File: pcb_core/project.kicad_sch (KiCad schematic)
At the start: 55 parts, among them IC4 TCA9548APWR, J1 Conn_01x02, J19 Conn_02x02_Counter_Clockwise, J2 1725656, J20 PCBConnector, J21 PCBConnector, J22 PCBConnector, J23 PCBConnector, J25 PCBConnector, J27 PCBConnector, Q1 SI9945BDY-T1-GE3, U1 ESP32-S3-WROOM-2, U2 LTC4365TS8, U3 ESP32-DevKitC

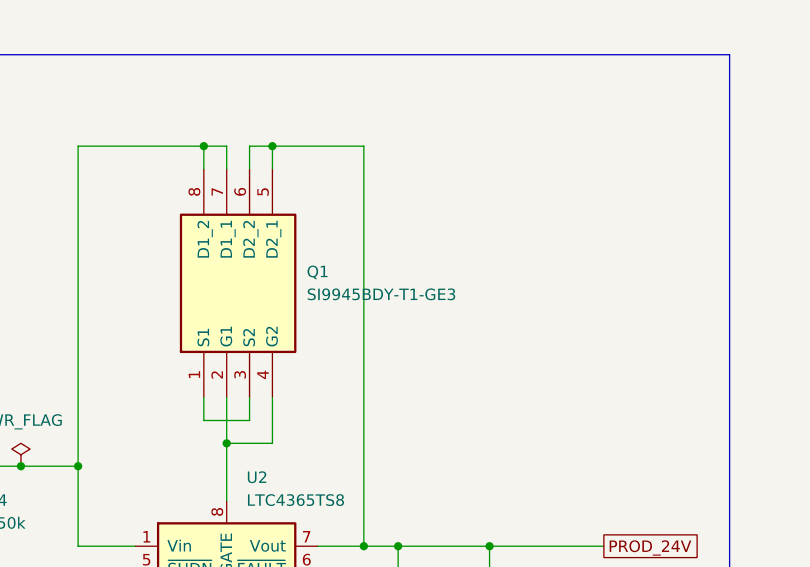
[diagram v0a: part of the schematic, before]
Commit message: Change to I4214DDY-T1-GE3 and update PCB
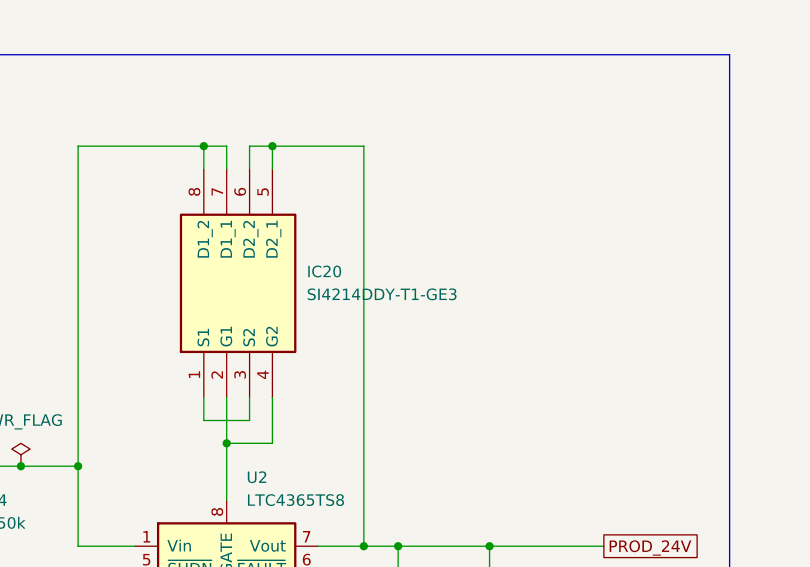
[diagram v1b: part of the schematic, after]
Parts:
- removed Q1: SI9945BDY-T1-GE3, library:SOIC127P600X175-8N, symbol SI9945BDY-T1-GE3:SI9945BDY-T1-GE3
- added IC20: SI4214DDY-T1-GE3, library:SOIC127P600X175-8N, symbol SI4214DDY-T1-GE3:SI4214DDY-T1-GE3
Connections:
- net PROD_24V: now also IC20.5 (D2_1), IC20.6 (D2_2)
- net VIN_24V: now also IC20.7 (D1_1), IC20.8 (D1_2)
- net at U2.8 (GATE): now also IC20.2 (G1), IC20.4 (G2)
- new net: IC20.1 (S1), IC20.3 (S2)
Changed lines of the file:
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@@
 	)
 	(symbol
+		(lib_id "SI4214DDY-T1-GE3:SI4214DDY-T1-GE3")
+		(at 140.97 344.17 90)
+		(unit 1)
+		(exclude_from_sim no)
+		(in_bom yes)
+		(on_board yes)
+		(dnp no)
+		(fields_autoplaced yes)
+		(property "Reference" "IC20"
+			(at 152.4 330.1999 90)
+			(effects
+				(font
+					(size 1.27 1.27)
+				)
+				(justify right)
+			)
+		)
+		(property "Value" "SI4214DDY-T1-GE3"
+			(at 152.4 332.7399 90)
+			(effects
+				(font
+					(size 1.27 1.27)
+				)
+				(justify right)
+			)
+		)
+		(property "Footprint" "library:SOIC127P600X175-8N"
+			(at 235.89 322.58 0)
+			(effects
+				(font
+					(size 1.27 1.27)
+				)
+				(justify left top)
+				(hide yes)
+			)
+		)
+		(property "Datasheet" "https://www.vishay.com/docs/65022/si4214ddy.pdf"
+			(at 335.89 322.58 0)
+			(effects
+				(font
+					(size 1.27 1.27)
+				)
+				(justify left top)
+				(hide yes)
+			)
+		)
+		(property "Description" "SI4214DDY-T1-GE3, Dual N-channel MOSFET Transistor 7.5A 30V, 8-Pin SOIC"
+			(at 140.97 344.17 0)
+			(effects
+				(font
+					(size 1.27 1.27)
+				)
+				(hide yes)
+			)
+		)
+		(property "Height" "1.75"
+			(at 535.89 322.58 0)
+			(effects
+				(font
+					(size 1.27 1.27)
+				)
+				(justify left top)
+				(hide yes)
+			)
+		)
+		(property "Mouser Part Number" "781-SI4214DDY-GE3"
+			(at 635.89 322.58 0)
+			(effects
+				(font
+					(size 1.27 1.27)
+				)
+				(justify left top)
+				(hide yes)
+			)
+		)
+		(property "Mouser Price/Stock" "https://www.mouser.co.uk/ProductDetail/Vishay-Semiconductors/SI4214DDY-T1-GE3?qs=kt16UJ73eEGZKWuc2RKrng%3D%3D"
+			(at 735.89 322.58 0)
+			(effects
+				(font
+					(size 1.27 1.27)
+				)
+				(justify left top)
+				(hide yes)
+			)
+		)
+		(property "Manufacturer_Name" "Vishay"
+			(at 835.89 322.58 0)
+			(effects
+				(font
+					(size 1.27 1.27)
+				)
+				(justify left top)
+				(hide yes)
+			)
+		)
+		(property "Manufacturer_Part_Number" "SI4214DDY-T1-GE3"
+			(at 935.89 322.58 0)
+			(effects
+				(font
+					(size 1.27 1.27)
+				)
+				(justify left top)
+				(hide yes)
+			)
+		)
+		(property "LCSC#" "C553963"
+			(at 140.97 344.17 0)
+			(effects
+				(font
+					(size 1.27 1.27)
+				)
+				(hide yes)
+			)
+		)
+		(property "Config" "-SubNode "
+			(at 140.97 344.17 0)
+			(effects
+				(font
+					(size 1.27 1.27)
+				)
+				(hide yes)
+			)
+		)
+		(pin "6"
+		)
+		(pin "7"
+		)
+		(pin "1"
+		)
+		(pin "4"
+		)
+		(pin "3"
+		)
+		(pin "2"
+		)
+		(pin "8"
+		)
+		(pin "5"
+		)
+		(instances
+			(project "project"
+				(path "/97ee99f6-6664-45d1-b5d6-247aaf34e934"
+					(reference "IC20")
+					(unit 1)
+				)
+			)
+		)
+	)
+	(symbol
 		(lib_id "power:PWR_FLAG")
 		(at 120.65 25.4 0)
@@
 					(unit 1)
 				)
-			)
-		)
-	)
-	(symbol
-		(lib_id "SI9945BDY-T1-GE3:SI9945BDY-T1-GE3")
-		(at 140.97 344.17 90)
-		(unit 1)
-		(exclude_from_sim no)
-		(in_bom yes)
-		(on_board yes)
-		(dnp no)
-		(fields_autoplaced yes)
-		(property "Reference" "Q1"
-			(at 152.4 330.1999 90)
-			(effects
-				(font
-					(size 1.27 1.27)
-				)
-				(justify right)
-			)
-		)
-		(property "Value" "SI9945BDY-T1-GE3"
-			(at 152.4 332.7399 90)
-			(effects
-				(font
-					(size 1.27 1.27)
-				)
-				(justify right)
-			)
-		)
-		(property "Footprint" "library:SOIC127P600X175-8N"
-			(at 235.89 322.58 0)
-			(effects
-				(font
-					(size 1.27 1.27)
-				)
-				(justify left top)
-				(hide yes)
-			)
-		)
-		(property "Datasheet" ""
-			(at 335.89 322.58 0)
-			(effects
-				(font
-					(size 1.27 1.27)
-				)
-				(justify left top)
-				(hide yes)
-			)
-		)
-		(property "Description" "Vishay SI9945BDY-T1-GE3 Dual N-channel MOSFET Transistor, 5.3 A, 60 V, 8-Pin SOIC"
-			(at 140.97 344.17 0)
-			(effects
-				(font
-					(size 1.27 1.27)
-				)
-				(hide yes)
-			)
-		)
-		(property "Height" "1.75"
-			(at 535.89 322.58 0)
-			(effects
-				(font
-					(size 1.27 1.27)
-				)
-				(justify left top)
-				(hide yes)
-			)
-		)
-		(property "Mouser Part Number" "781-SI9945BDY-GE3"
-			(at 635.89 322.58 0)
-			(effects
-				(font
-					(size 1.27 1.27)
-				)
-				(justify left top)
-				(hide yes)
-			)
-		)
-		(property "Manufacturer_Name" "Vishay"
-			(at 835.89 322.58 0)
-			(effects
-				(font
-					(size 1.27 1.27)
-				)
-				(justify left top)
-				(hide yes)
-			)
-		)
-		(property "Manufacturer_Part_Number" "SI9945BDY-T1-GE3"
-			(at 935.89 322.58 0)
-			(effects
-				(font
-					(size 1.27 1.27)
-				)
-				(justify left top)
-				(hide yes)
-			)
-		)
-		(property "LCSC#" "C435838"
-			(at 140.97 344.17 0)
-			(effects
-				(font
-					(size 1.27 1.27)
-				)
-				(hide yes)
-			)
-		)
-		(property "Config" "-SubNode "
-			(at 140.97 344.17 0)
-			(effects
-				(font
-					(size 1.27 1.27)
-				)
-				(hide yes)
-			)
-		)
-		(property "LCSC# Alt1" ""
-			(at 140.97 344.17 0)
-			(effects
-				(font
-					(size 1.27 1.27)
-				)
-				(hide yes)
-			)
-		)
-		(pin "8"
-		)
-		(pin "7"
-		)
-		(pin "6"
-		)
-		(pin "5"
-		)
-		(pin "1"
-		)
-		(pin "4"
-		)
-		(pin "3"
-		)
-		(pin "2"
-		)
-		(instances
-			(project "project"
-				(path "/97ee99f6-6664-45d1-b5d6-247aaf34e934"
-					(reference "Q1")
-					(unit 1)
-				)

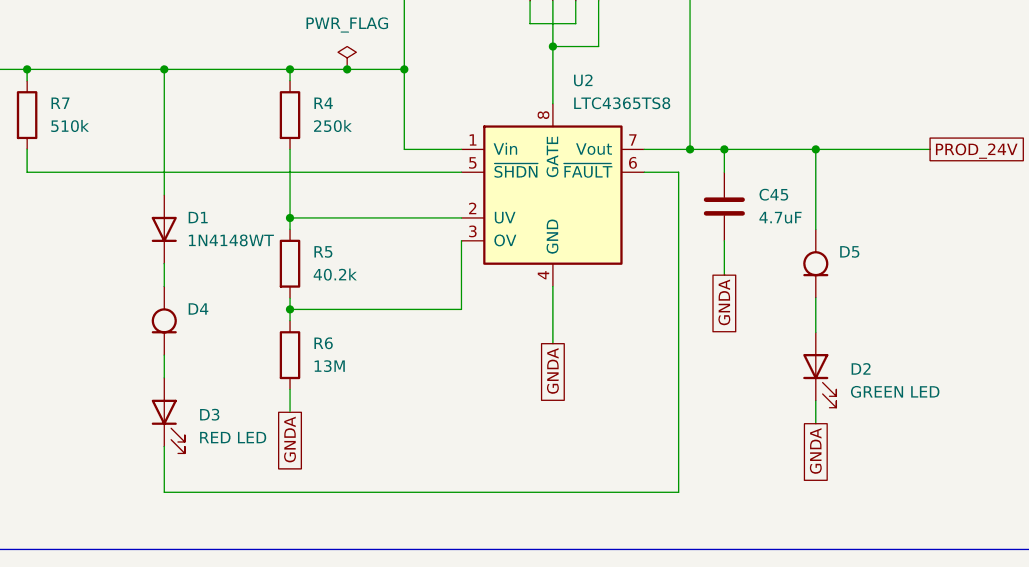
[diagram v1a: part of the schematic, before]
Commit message: Correct schematic symbol for Current Regulator Diodes, Update Kibot config
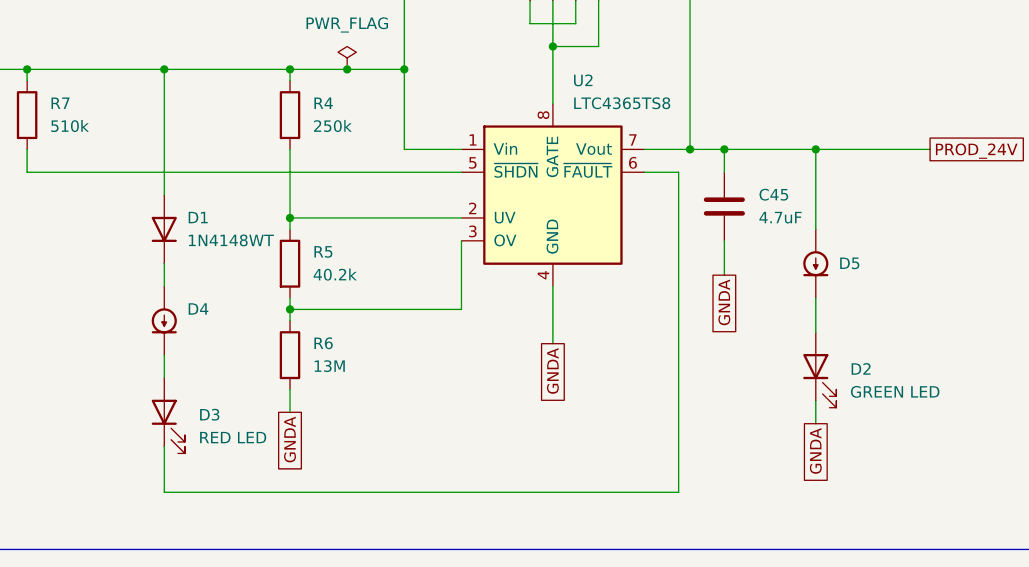
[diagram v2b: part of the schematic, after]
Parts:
- D4, D5: symbol Device:D_Constant_Current -> Device:D_Current-regulator
- IC20, PS1, R4, R5, R6, R7, U2: Config -SubNode -> -SubNode
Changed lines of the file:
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@@
 			)
 		)
-		(property "Config" "-SubNode "
+		(property "Config" "-SubNode"
 			(at 114.3 356.87 0)
 			(effects
@@
 	)
 	(symbol
-		(lib_id "Device:D_Constant_Current")
+		(lib_id "Device:D_Current-regulator")
 		(at 100.33 379.73 90)
 		(unit 1)
@@
 		)
 		(property "Footprint" "Diode_SMD:D_SOD-123F"
-			(at 96.266 379.73 0)
+			(at 100.33 379.603 0)
 			(effects
 				(font
@@
 			)
 		)
-		(property "Description" "DIODE, CURRENT LIMITING, 2.3V, 500mW, SOD-123FL"
+		(property "Description" "Constant-current diode / current limiting diode / current regulator diode, IEC60747-3:2013"
 			(at 100.33 379.73 0)
 			(effects
@@
 			)
 		)
-		(property "Config" "-SubNode "
+		(property "Config" "-SubNode"
 			(at 143.51 365.76 0)
 			(effects
@@
 			)
 		)
-		(property "Config" "-SubNode "
+		(property "Config" "-SubNode"
 			(at 140.97 344.17 0)
 			(effects
@@
 			)
 		)
-		(property "Config" "-SubNode "
+		(property "Config" "-SubNode"
 			(at 114.3 373.38 0)
 			(effects
@@
 			)
 		)
-		(property "Config" "-SubNode "
+		(property "Config" "-SubNode"
 			(at 396.24 344.17 0)
 			(effects
@@
 			)
 		)
-		(property "Config" "-SubNode "
+		(property "Config" "-SubNode"
 			(at 85.09 356.87 0)
 			(effects
@@
 			)
 		)
-		(property "Config" "-SubNode "
+		(property "Config" "-SubNode"
 			(at 114.3 383.54 0)
 			(effects
@@
 			)
 		)
-		(property "Description" "Standard LEDs - SMD Green 560nm 54mW "
+		(property "Description" "Standard LEDs - SMD Green 560nm 54mW"
 			(at 172.72 384.81 0)
 			(effects
@@
 			)
 		)
-		(property "Description" "Standard LEDs - SMD Green 560nm 54mW "
+		(property "Description" "Standard LEDs - SMD Green 560nm 54mW"
 			(at 365.76 370.84 0)
 			(effects
@@
 	)
 	(symbol
-		(lib_id "Device:D_Constant_Current")
+		(lib_id "Device:D_Current-regulator")
 		(at 172.72 373.38 90)
 		(unit 1)
@@
 		(fields_autoplaced yes)
 		(property "Reference" "D5"
-			(at 175.26 372.1099 90)
+			(at 175.26 373.3799 90)
 			(effects
 				(font
@@
 		)
 		(property "Footprint" "Diode_SMD:D_SOD-123F"
-			(at 172.72 373.38 0)
+			(at 172.72 373.253 0)
 			(effects
 				(font
@@
 			)
 		)
-		(property "Description" "DIODE, CURRENT LIMITING, 2.3V, 500mW, SOD-123FL"
+		(property "Description" "Constant-current diode / current limiting diode / current regulator diode, IEC60747-3:2013"
 			(at 172.72 373.38 0)
 			(effects

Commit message: Add AISLER bom support and assigned components
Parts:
- C1, C11: AISLER_MPN (none) -> 10.0µF, 1206 SMD
- C2, C3, C4: AISLER_MPN (none) -> 100.0nF, 1206 SMD
- C42: AISLER_MPN (none) -> FZ47UF35V90RV0124; Manufacturer_Name (none) -> KNSCHA; Manufacturer_Part_Number Polarized Capacitor, 47.0uF, 35V, D6.3xL7.7 SMD -> FZ47UF35V90RV0124
- C45: AISLER_MPN (none) -> C45 4.7µF, 0805 SMD
- C5: AISLER_MPN (none) -> 1.0µF, 1206 SMD
- D1: AISLER_MPN (none) -> 1N4148WT
- D2, D6: AISLER_MPN (none) -> SML-012P8TT86
- D3: AISLER_MPN (none) -> SML-012V8TT86
- D4, D5: AISLER_MPN (none) -> CMJ2000 TR PBFREE
- IC20: AISLER_MPN (none) -> SI4214DDY-T1-GE3
- IC4: AISLER_MPN (none) -> TCA9548APWR
- J2: AISLER_MPN (none) -> 1725656
- PS1: AISLER_MPN (none) -> PQQ10W-Q24-S3-S
- R16, R2: AISLER_MPN (none) -> 10.0kΩ, 1206 SMD
- R23: AISLER_MPN (none) -> 56.0Ω, 1206 SMD
- R3: AISLER_MPN (none) -> 0.0Ω, 1206 SMD
- R5: AISLER_MPN (none) -> 40.2kΩ, 1206 SMD
- R7: AISLER_MPN (none) -> 510.0kΩ, 1206 SMD
- S1, S2: AISLER_MPN (none) -> EVP-3AA02Q
- S3: AISLER_MPN (none) -> A6S-3102-PH
- U1: AISLER_MPN (none) -> ESP32-S3-WROOM-2-N32R8V
- U2: AISLER_MPN (none) -> LTC4365CTS8#TRMPBF
- U3: AISLER_MPN (none) -> ESP32-DevKitC

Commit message: Update BOM Mouser
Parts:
- C1, C11: Manufacturer_Part_Number (none) -> Capacitor, 10uF, 1206 SMD; Mouser Part Number (none) -> 187-CL31B106KOHNNWE
- C2, C3, C4: Mouser Part Number (none) -> 80-C1206C104M5R
- C41: Mouser Part Number (none) -> 710-865080745011
- C42: Mouser Part Number (none) -> 710-865090545008
- C45: Manufacturer_Part_Number (none) -> Capacitor, 4.7uF, 0805 SMD; Mouser Part Number (none) -> 187-CL21A475KAQNNNE
- C5: Mouser Part Number (none) -> 80-C1206C105K4RAC
- PS1: Mouser# Alt1 (none) -> 709-SPBW06F-03
- R13, R14, R15, R17, R19, R20: Mouser Part Number (none) -> 71-CRCW12065K10FKEAC
- R16, R2: Mouser Part Number (none) -> 603-RC1206FR-1010KL
- R23: Mouser Part Number (none) -> 71-CRCW1206-56-E3
- R3: Mouser Part Number (none) -> 71-CRCW12060000Z0EC
- R4: Mouser Part Number (none) -> 652-CR1206FX-2553ELF
- R5: Mouser Part Number (none) -> 660-RK73H2BTTD4022F
- R6: Mouser Part Number (none) -> 660-RK73B2BTTD136J
- R7: Mouser Part Number (none) -> 71-CRCW1206-510K-E3
- S3: Mouser# Alt1 (none) -> 653-A6S-3102-H

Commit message: New package version of model train controller
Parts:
- removed C1: 10uF, Capacitor_SMD:C_1206_3216Metric_Pad1.33x1.80mm_HandSolder, symbol Device:C
- removed C11: 10uF, Capacitor_SMD:C_1206_3216Metric_Pad1.33x1.80mm_HandSolder, symbol Device:C_Small
- removed C2, C3, C4: 0.1uF, Capacitor_SMD:C_1206_3216Metric_Pad1.33x1.80mm_HandSolder, symbol Device:C
- removed C45: 4.7uF, Capacitor_SMD:C_0805_2012Metric_Pad1.18x1.45mm_HandSolder, symbol Device:C
- removed C5: 1uF, Capacitor_SMD:C_1206_3216Metric_Pad1.33x1.80mm_HandSolder, symbol Device:C
- removed D1: 1N4148WT, Diode_SMD:D_SOD-523, symbol Diode:1N4148WT
- removed D3: RED LED, LED_SMD:LED_1206_3216Metric_Pad1.42x1.75mm_HandSolder, symbol Device:LED
- removed D4: ~, Diode_SMD:D_SOD-123F, symbol Device:D_Current-regulator
- removed IC20: SI4214DDY-T1-GE3, library:SOIC127P600X175-8N, symbol SI4214DDY-T1-GE3:SI4214DDY-T1-GE3
- removed IC4: TCA9548APWR, library:SOP65P640X120-24N, symbol TCA9548APWR:TCA9548APWR
- removed J1: Conn_01x02, Connector_PinHeader_2.54mm:PinHeader_1x02_P2.54mm_Vertical, symbol Connector_Generic:Conn_01x02
- removed J19: Conn_02x02_Counter_Clockwise, Connector_PinHeader_2.54mm:PinHeader_2x02_P2.54mm_Vertical_SMD, symbol Connector_Generic:Conn_02x02_Counter_Clockwise
- removed J23: PCBConnector, TestPoint:TestPoint_THTPad_D3.0mm_Drill1.5mm, symbol Connector_Generic:Conn_01x01
- removed R13, R14, R15, R17, R19, R20: 5k, Resistor_SMD:R_1206_3216Metric_Pad1.30x1.75mm_HandSolder, symbol Device:R
- removed R16: 10k, Resistor_SMD:R_1206_3216Metric_Pad1.30x1.75mm_HandSolder, symbol Device:R_Small
- removed R2: 10k, Resistor_SMD:R_1206_3216Metric_Pad1.30x1.75mm_HandSolder, symbol Device:R
- removed R3: 0, Resistor_SMD:R_1206_3216Metric_Pad1.30x1.75mm_HandSolder, symbol Device:R
- removed R4: 250k, Resistor_SMD:R_1206_3216Metric_Pad1.30x1.75mm_HandSolder, symbol Device:R
- removed R5: 40.2k, Resistor_SMD:R_1206_3216Metric_Pad1.30x1.75mm_HandSolder, symbol Device:R
- removed R6: 13M, Resistor_SMD:R_1206_3216Metric_Pad1.30x1.75mm_HandSolder, symbol Device:R
- removed R7: 510k, Resistor_SMD:R_1206_3216Metric_Pad1.30x1.75mm_HandSolder, symbol Device:R
- removed S1, S2: EVP-3AA02Q, library:EVP3AA02Q, symbol EVP-3AA02Q:EVP-3AA02Q
- removed S3: A6S-3102-PH, library:A6S3102PH, symbol A6S-3102-PH:A6S-3102-PH
- removed U1: ESP32-S3-WROOM-2, PCM_Espressif:ESP32-S3-WROOM-2, symbol Espressif:ESP32-S3-WROOM-2
- removed U2: LTC4365TS8, Package_TO_SOT_SMD:TSOT-23-8, symbol Power_Management:LTC4365TS8
- removed U3: ESP32-DevKitC, PCM_Espressif:ESP32-DevKitC, symbol Espressif:ESP32-DevKitC
- added J1: PCBConnector, TestPoint:TestPoint_THTPad_D3.0mm_Drill1.5mm, symbol Connector_Generic:Conn_01x01
- added U1: ~, cust_pcb:esp32, symbol cust_pcb:esp32
- added U2: ~, cust_pcb:voltage_protection, symbol cust_pcb:voltage_protection
- added U4, U5: ~, cust_pcb:ioexpander, symbol cust_pcb:ioexpander
- added U6: ~, cust_pcb:i2cmultiplexer, symbol cust_pcb:i2cmultiplexer
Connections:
- net 24V: now also U2.7 (VCC), U2.8 (VCC), U2.9 (VCC); no longer J20.1 (Pin_1)
- net ESP32_SCL: now also J1.1 (Pin_1), U1.2 (SCL), U6.3 (SCL)
- net ESP32_SDA: now also U1.1 (SDA), U6.4 (SDA)
- net GNDA: now also C42.2, U2.1 (GNDA), U2.10 (GNDA), U2.11 (GNDA), U2.12 (GNDA), U2.2 (GNDA), U2.3 (GNDA); no longer C42.1
- net GNDD: now also U1.10 (GNDD), U1.11 (GNDD), U1.12 (GNDD), U1.13 (GNDD), U1.14 (GNDD), U1.15 (GNDD), U1.16 (GNDD), U1.17 (GNDD), U1.3 (GNDD), U1.4 (GNDD), U1.5 (GNDD), U1.6 (GNDD), U1.7 (GNDD), U1.8 (GNDD), U1.9 (GNDD), U4.2 (GNDD), U4.32 (GNDD), U4.42 (GNDD), U5.2 (GNDD), U5.32 (GNDD), U5.42 (GNDD), U6.2 (GNDD)
- net IN1_1: now also U5.14 (IO14)
- net IN1_10: now also U4.16 (IO12)
- net IN1_11: now also U4.18 (IO10)
- net IN1_12: now also U4.20 (IO08)
- net IN1_13: now also U4.6 (IO01)
- net IN1_14: now also U4.8 (IO03)
- net IN1_15: now also U4.10 (IO05)
- net IN1_16: now also U4.12 (IO07)
- net IN1_2: now also U5.16 (IO12)
- net IN1_3: now also U5.19 (IO09)
- net IN1_4: now also U5.17 (IO11)
- net IN1_5: now also U5.11 (IO06)
- net IN1_6: now also U5.9 (IO04)
- net IN1_7: now also U5.7 (IO02)
- net IN1_8: now also U5.5 (IO00)
- net IN1_9: now also U4.14 (IO14)
- net IN2_1: now also U5.13 (IO15)
- net IN2_10: now also U4.15 (IO13)
- net IN2_11: now also U4.17 (IO11)
- net IN2_12: now also U4.19 (IO09)
- net IN2_13: now also U4.5 (IO00)
- net IN2_14: now also U4.7 (IO02)
- net IN2_15: now also U4.9 (IO04)
- net IN2_16: now also U4.11 (IO06)
- net IN2_2: now also U5.15 (IO13)
- net IN2_3: now also U5.20 (IO08)
- net IN2_4: now also U5.18 (IO10)
- net IN2_5: now also U5.12 (IO07)
- net IN2_6: now also U5.10 (IO05)
- net IN2_7: now also U5.8 (IO03)
- net IN2_8: now also U5.6 (IO01)
- net IN2_9: now also U4.13 (IO15)
- net IOEXP01_SCL: now also U4.3 (SCL), U6.7 (SC0)
- net IOEXP01_SDA: now also U4.4 (SDA), U6.6 (SD0)
- net IOEXP02_SCL: now also U5.3 (SCL), U6.13 (SC3)
- net IOEXP02_SDA: now also U5.4 (SDA), U6.12 (SD3)
- net PROD_24V: now also C42.1, J20.1 (Pin_1), U2.4 (VPC), U2.5 (VPC), U2.6 (VPC); no longer C42.2
- net VCC_3V3: now also U1.18 (VCC), U4.31 (VCC), U5.1 (VCC), U6.1 (VCC)
- no-connect marks 77 -> 20
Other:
- removed sheet IOExpander1
- removed sheet IOExpander2
- note removed: "I²C Multiplexer"
- note removed: "Voltage Protection"
- note removed: "https://www.analog.com/media/en/technical-documentation/eval-board-schematic/DC1555C-2-SCH.PDF"
- moved on the sheet: C41, D2, D5, D6, J2, J20, J21, J25, J27, PS1, R23

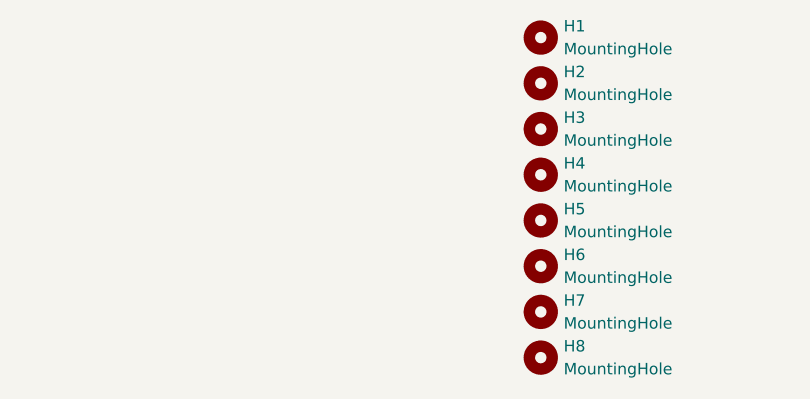
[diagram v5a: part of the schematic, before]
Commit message: Add Panelize connector to PCB_Core
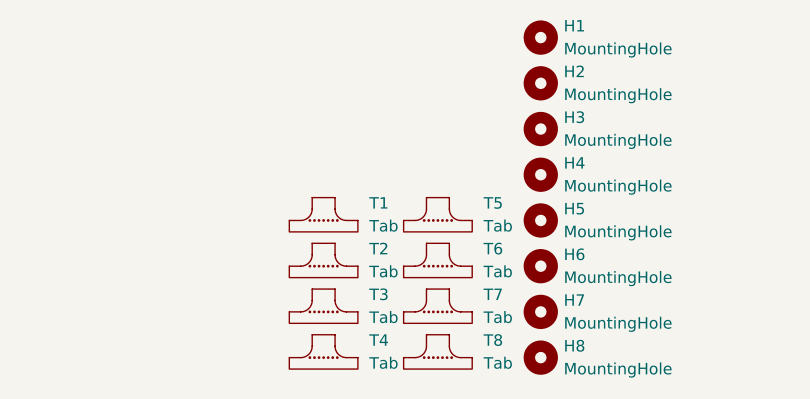
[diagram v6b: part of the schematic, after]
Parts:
- added T1, T2, T3, T4, T5, T6, T7, T8: Tab, PCM_kikit:Tab, symbol PCM_kikit:Tab
